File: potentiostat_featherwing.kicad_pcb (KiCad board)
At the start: 2 copper layers, 16 parts, among them J1 Screw_Terminal_01x03, P1 pin_array_3x1, U1 feather_wing, U2 LMP7721, U3 LMP7721, U4 LMP7721, U5 LMP7721

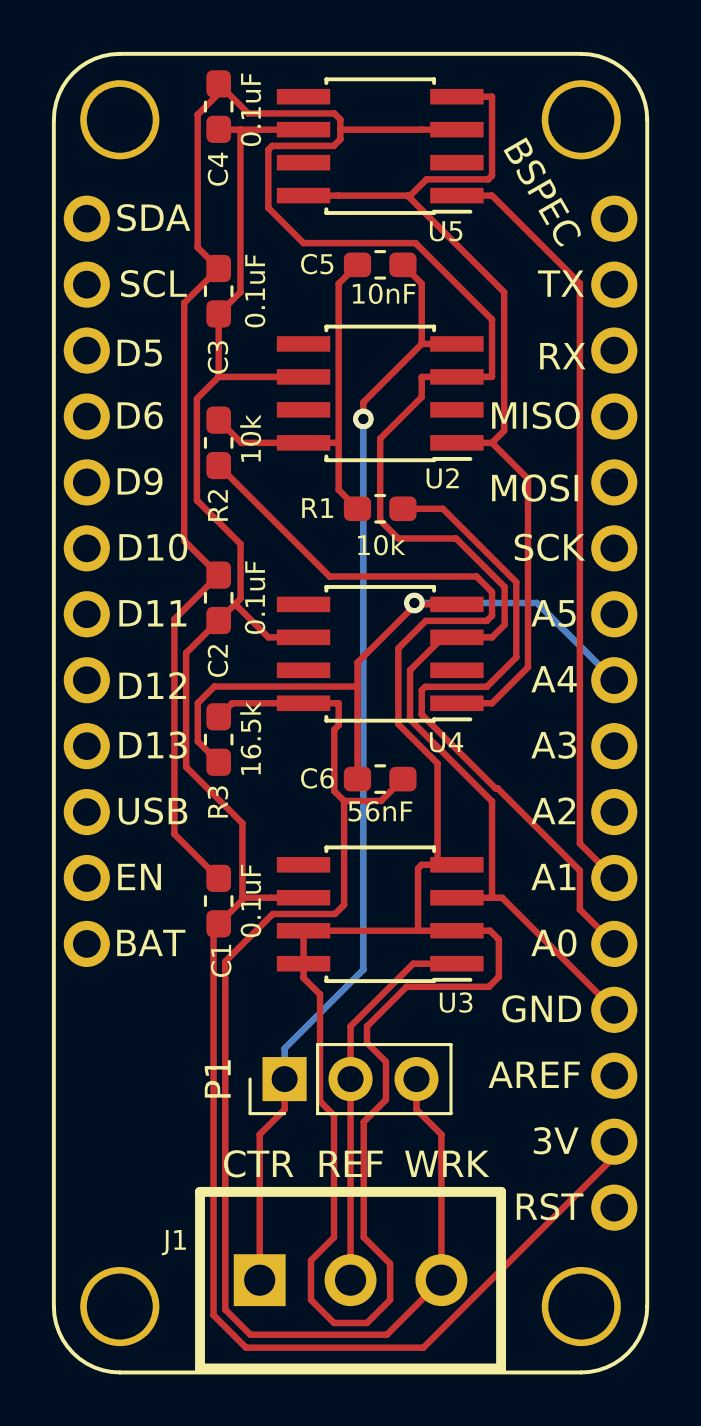
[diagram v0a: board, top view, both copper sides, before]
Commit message: Modified design so that ref elect (buffered) can be measured by analog input.
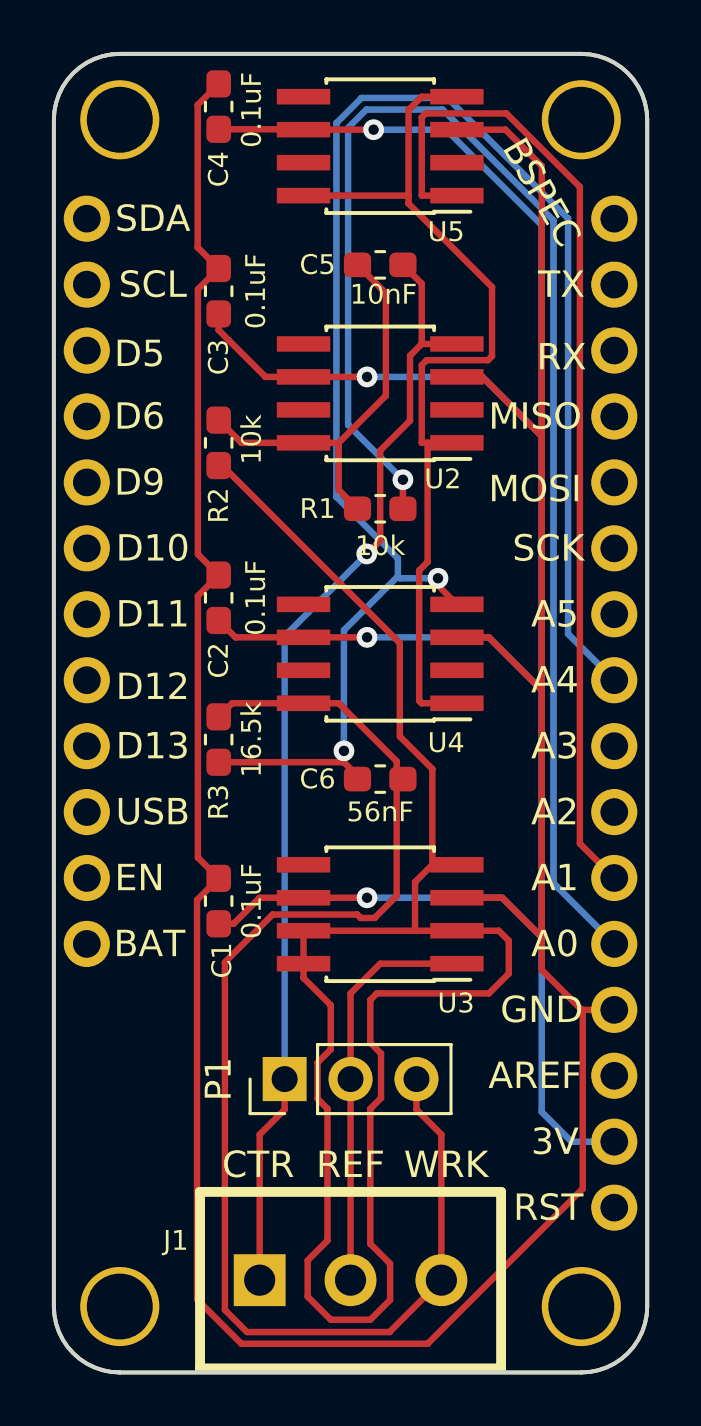
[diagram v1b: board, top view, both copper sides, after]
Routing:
- net /AIN_TIA: track 27.3 -> 64.8 mm, vias 1 -> 2
- net /DAC_SETPT: track 25.5 -> 54.4 mm, vias 0 -> 1
- net GND: track 100.5 -> 124.7 mm
- net /3V3: track 80.9 -> 93.2 mm, vias 0 -> 4
- net /DAC_VGND: track 29.6 -> 38.9 mm
- net /REF_ELECT_BUF: track 76.7 -> 69.0 mm
- net /VGND: track 37.1 -> 35.7 mm
- net Net-(C5-Pad2): track 15.0 -> 15.9 mm
- net /REF_ELECT: track 14.9 -> 15.6 mm
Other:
- board outline added: 22.9 x 50.8 mm
